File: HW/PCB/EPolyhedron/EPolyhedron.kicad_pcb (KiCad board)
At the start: 2 copper layers, 29.7 x 47.5 mm, 62 parts, among them J1 piezoelectric element', J2 ISP, J3 Battery, U1 ATtiny24A-SSU, U2 CD74HC4511M, U3 CD74HC4511M, U4 LP3985

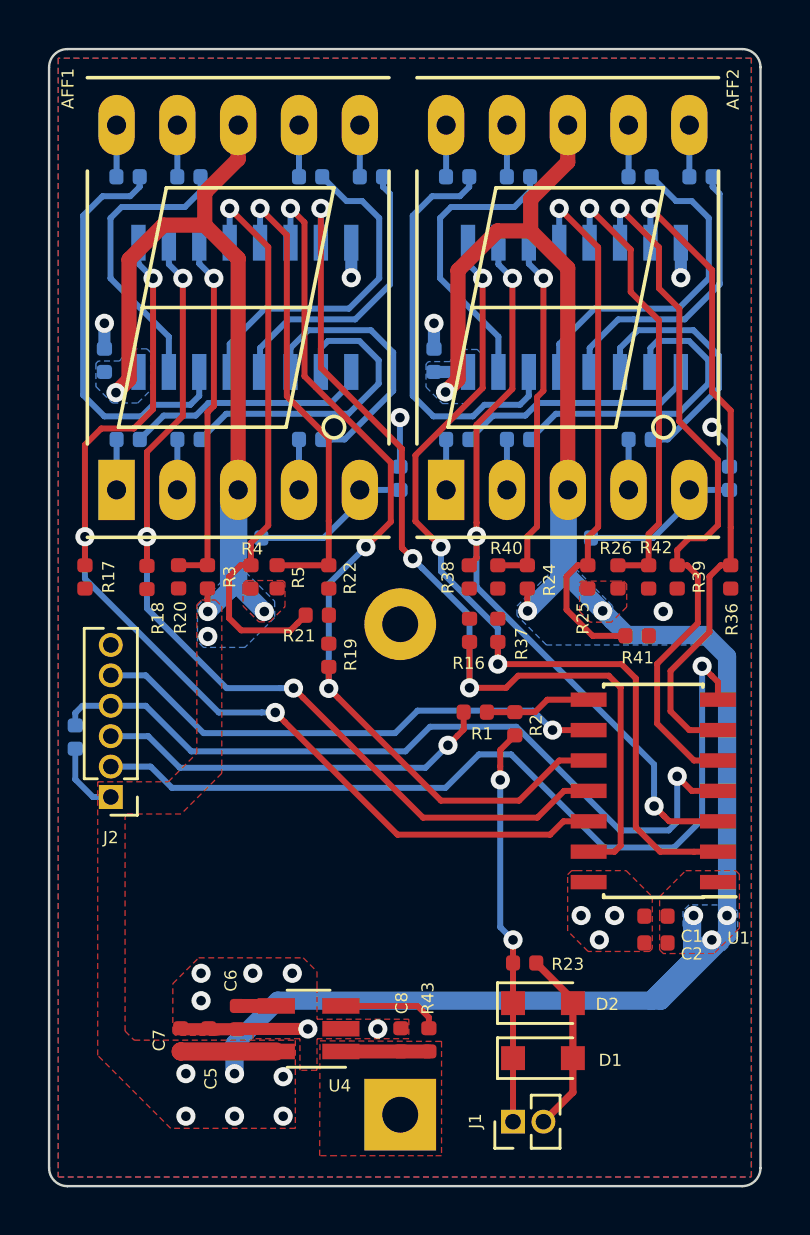
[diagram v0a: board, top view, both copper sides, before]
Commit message: Added d20 logo to silkscreen
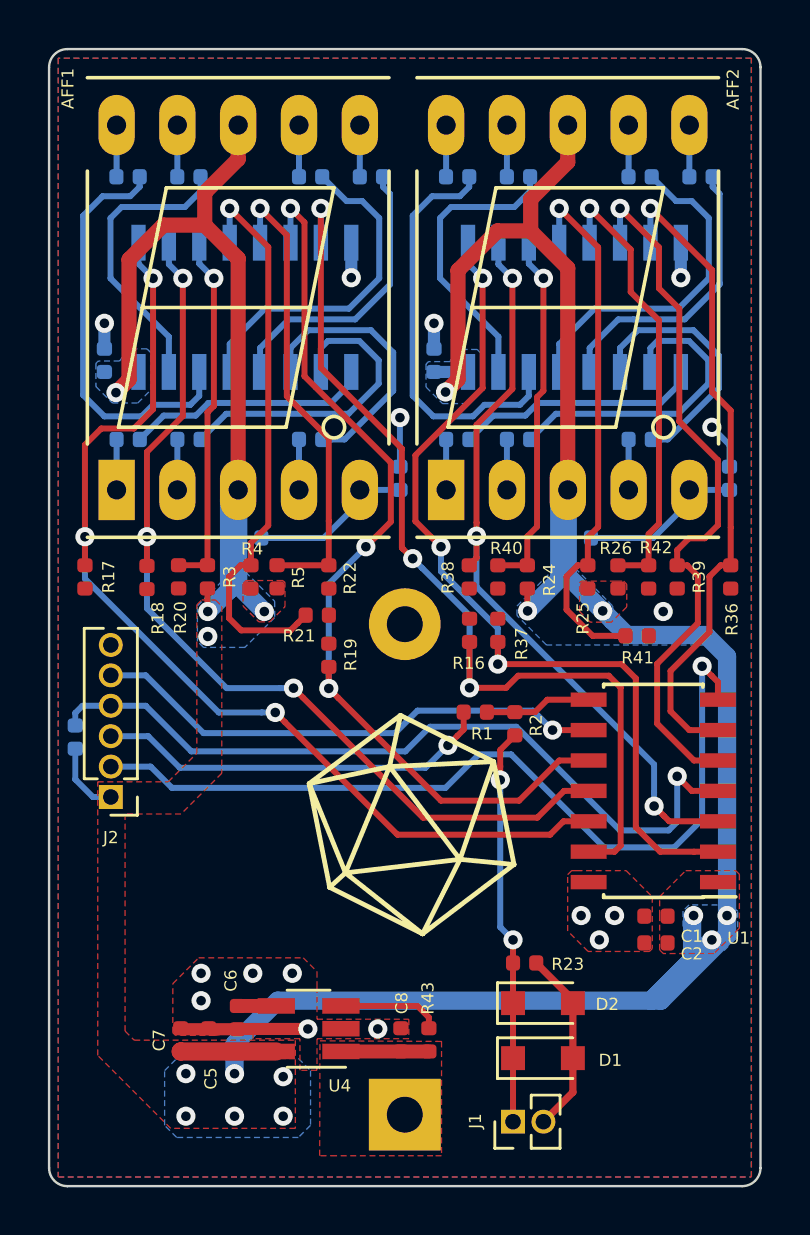
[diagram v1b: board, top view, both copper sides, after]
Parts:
- moved J3 0.19 mm to (88.5, 80.3)
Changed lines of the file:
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@@
   (general
     (thickness 1.6)
-    (drawings 13)
+    (drawings 31)
     (tracks 523)
     (zones 0)
@@
   )
   (setup
-    (last_trace_width 0.5842)
+    (last_trace_width 0.25)
     (user_trace_width 0.3048)
     (user_trace_width 0.381)
@@
   )
   (module Battery:BatteryHolder_Keystone_106_1x20mm (layer B.Cu)
-    (at 88.3285 80.3275 90)
+    (at 88.519 80.3275 90)
     (descr http://www.keyelco.com/product-pdf.cfm?p=720)
     (tags "Keystone type 106 battery holder")
@@
       (net 18 GND))
   )
+  (gr_line (start 84.524584 66.49886) (end 88.338364 63.646495) (layer F.SilkS) (width 0.2))
+  (gr_line (start 90.826126 69.66184) (end 89.262847 72.772697) (layer F.SilkS) (width 0.2))
+  (gr_line (start 93.081694 69.877315) (end 92.231277 65.579041) (layer F.SilkS) (width 0.2))
+  (gr_line (start 92.231277 65.579041) (end 88.338364 63.646495) (layer F.SilkS) (width 0.2))
+  (gr_line (start 85.380284 70.828817) (end 84.524584 66.49886) (layer F.SilkS) (width 0.2))
+  (gr_line (start 90.826126 69.66184) (end 93.081694 69.877315) (layer F.SilkS) (width 0.2))
+  (gr_line (start 88.338364 63.646495) (end 87.884 65.786) (layer F.SilkS) (width 0.2))
+  (gr_line (start 89.262847 72.772697) (end 93.081694 69.877315) (layer F.SilkS) (width 0.2))
+  (gr_line (start 92.231277 65.579041) (end 90.826126 69.66184) (layer F.SilkS) (width 0.2))
+  (gr_line (start 84.524584 66.49886) (end 86.040548 70.226848) (layer F.SilkS) (width 0.2))
+  (gr_line (start 90.826126 69.66184) (end 86.040548 70.226848) (layer F.SilkS) (width 0.2))
+  (gr_line (start 87.884 65.786) (end 84.524584 66.49886) (layer F.SilkS) (width 0.2))
+  (gr_line (start 89.262847 72.772697) (end 86.040548 70.226848) (layer F.SilkS) (width 0.2))
+  (gr_line (start 85.380284 70.828817) (end 89.262847 72.772697) (layer F.SilkS) (width 0.2))
+  (gr_line (start 87.884 65.786) (end 92.231277 65.579041) (layer F.SilkS) (width 0.2))
+  (gr_line (start 86.040548 70.226848) (end 85.380284 70.828817) (layer F.SilkS) (width 0.2))
+  (gr_line (start 86.040548 70.226848) (end 87.884 65.786) (layer F.SilkS) (width 0.2))
+  (gr_line (start 87.884 65.786) (end 90.826126 69.66184) (layer F.SilkS) (width 0.2))
+  (gr_line (start 102.616 35.814) (end 74.422 35.814) (layer Edge.Cuts) (width 0.1))
+  (gr_line (start 102.616 83.312) (end 74.422 83.312) (layer Edge.Cuts) (width 0.1))
   (gr_text 1 (at 269.8496 193.2178) (layer Dwgs.User)
     (effects (font (size 1.5 1.5) (thickness 0.3)))
@@
   (gr_arc (start 102.616 36.576) (end 103.378 36.576) (angle -90) (layer Edge.Cuts) (width 0.1))
   (gr_line (start 73.66 36.576) (end 73.66 82.55) (layer Edge.Cuts) (width 0.1))
-  (gr_line (start 102.616 83.312) (end 74.422 83.312) (layer Edge.Cuts) (width 0.1))
   (gr_line (start 103.378 36.576) (end 103.378 82.55) (layer Edge.Cuts) (width 0.1))
-  (gr_line (start 102.616 35.814) (end 74.422 35.814) (layer Edge.Cuts) (width 0.1))
   (segment (start 76.4794 52.1208) (end 76.4794 54.229) (width 0.25) (layer B.Cu) (net 1) (status 30))
   (segment (start 79.0194 52.1208) (end 79.0194 54.229) (width 0.25) (layer B.Cu) (net 2) (status 30))
@@
       )
     )
+  )
+  (zone (net 3) (net_name VDD) (layer B.Cu) (hatch edge 0.508)
+    (priority 1)
+    (connect_pads (clearance 0.127))
+    (min_thickness 0.254)
+    (fill yes (arc_segments 16) (thermal_gap 0.508) (thermal_bridge_width 0.508) (smoothing fillet) (radius 0.005))
+    (polygon
+      (pts
+        (xy 81.28 77.978) (xy 84.074 77.978) (xy 84.582 78.486) (xy 84.582 80.772) (xy 84.074 81.28)
+        (xy 78.994 81.28) (xy 78.486 80.772) (xy 78.486 78.486) (xy 78.994 77.978)
+      )
+    )
